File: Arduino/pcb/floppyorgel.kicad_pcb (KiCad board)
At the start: 2 copper layers, 50 x 50 mm, 46 parts, among them J1 VCC_Power_Select, J2 Floppy-Bus, J3 MAX485 Socket, J4 Floppy-Bus, J5 Buck-Converter-5V, J6 Buck-Converter-12V, J7 Floppy-Power, J8 IBM_PC_Floppy_IDC, J9 FTDI, SW1 Bus Address Select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

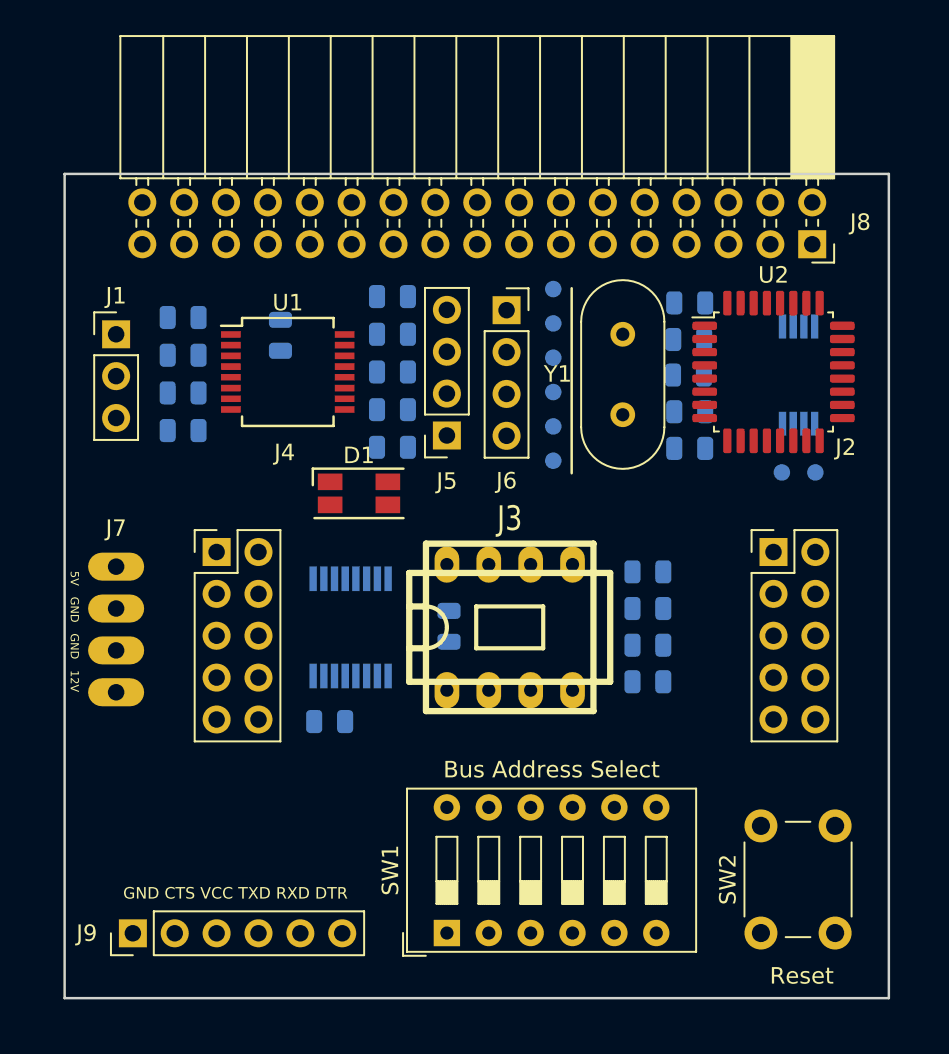
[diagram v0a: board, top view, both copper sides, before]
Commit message: pcb: add logo and zones
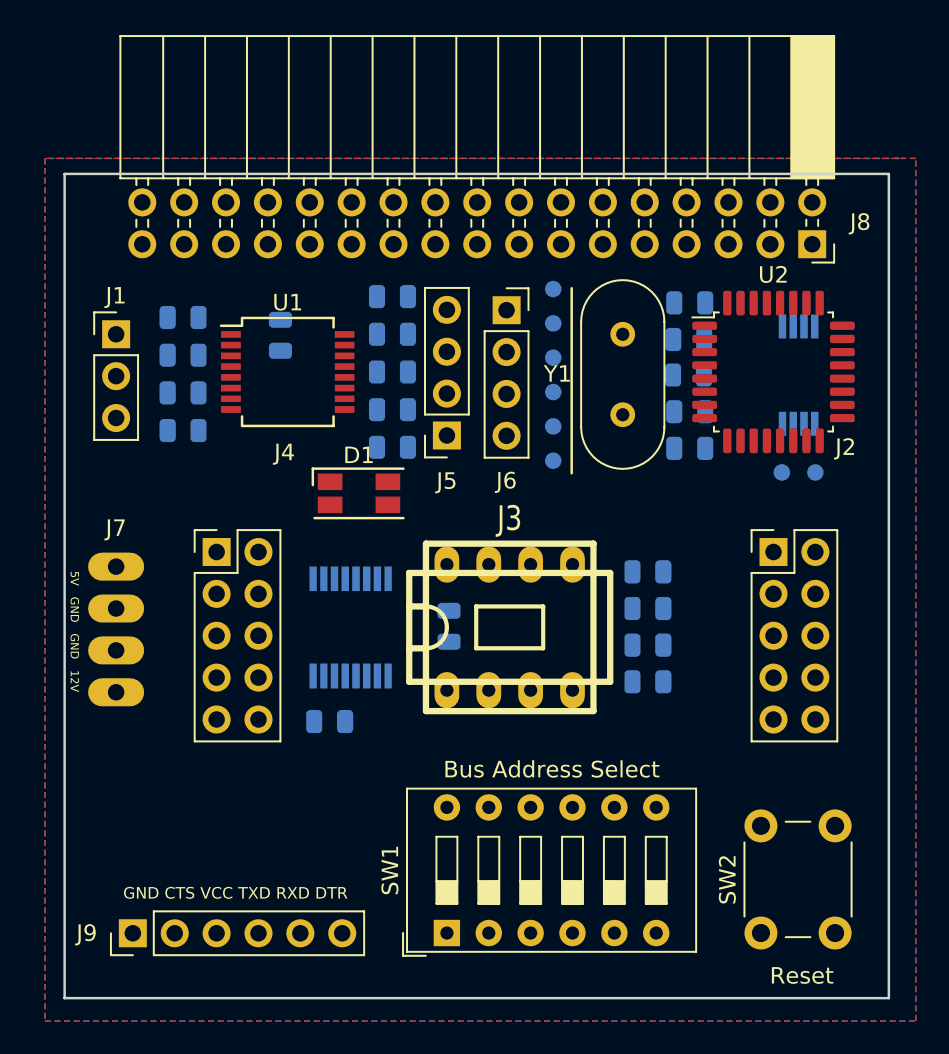
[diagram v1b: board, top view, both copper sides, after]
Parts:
- added G***: LOGO, logo:logo, B.Cu at (109.0, 138.7)
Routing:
- added copper zone on B.Cu, net GND
- added copper zone on F.Cu, net GND

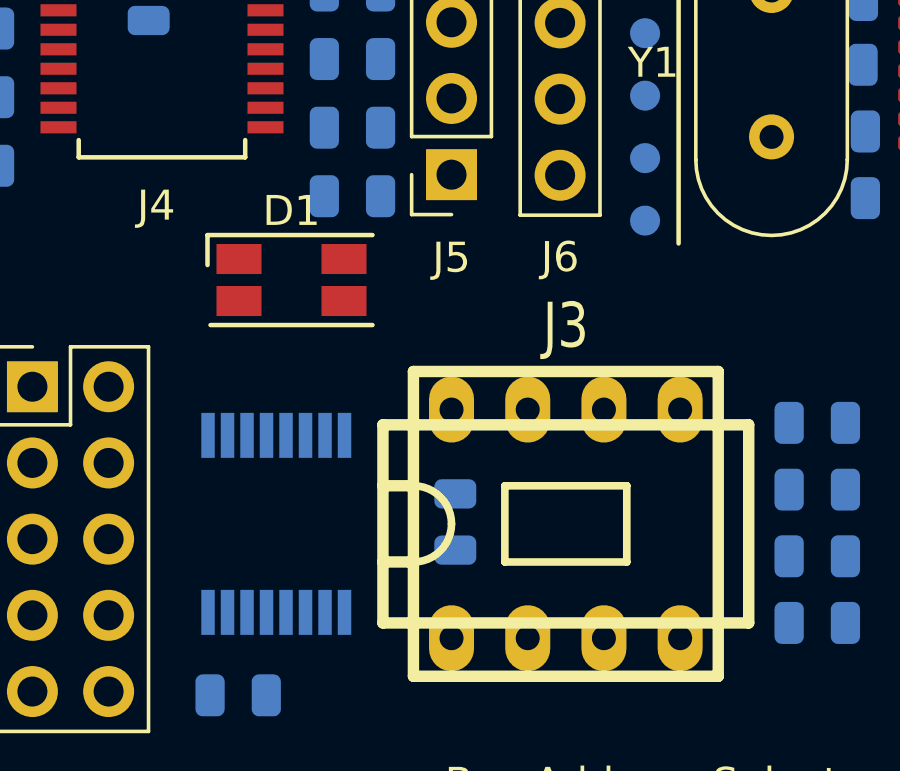
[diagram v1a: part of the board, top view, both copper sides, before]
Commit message: pcb: add missing footprints / add component for logo footprint
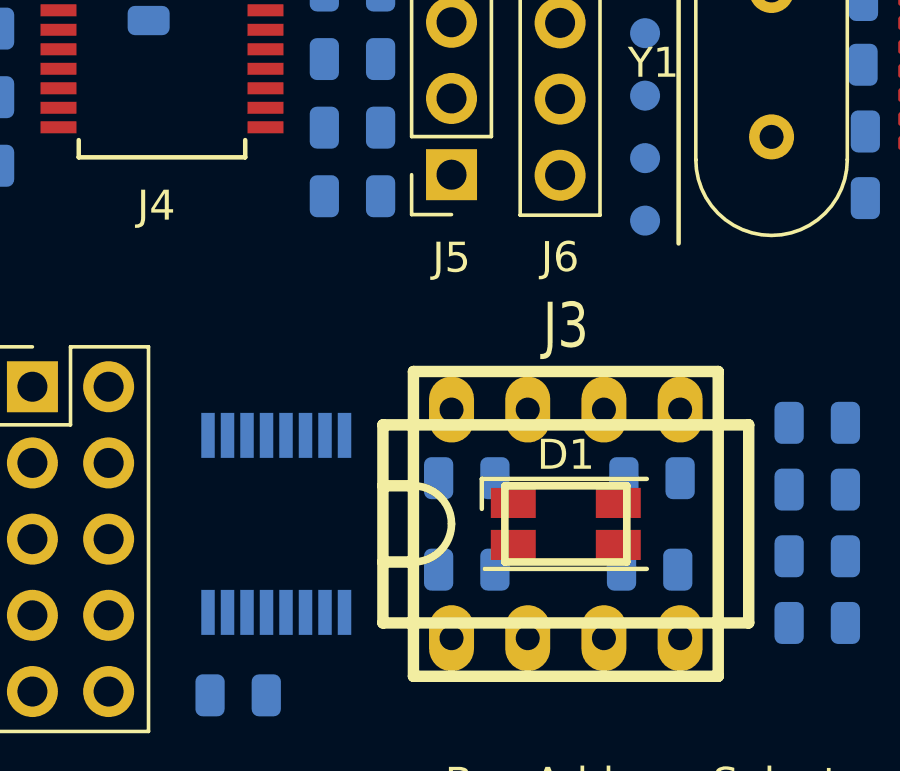
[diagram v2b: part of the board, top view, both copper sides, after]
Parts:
- removed G***: LOGO, logo:logo
- added R14: 250R, Resistor_SMD:R_0805_2012Metric, B.Cu at (123.7, 129.0)
- added R15: 250R, Resistor_SMD:R_0805_2012Metric, B.Cu at (129.8, 129.0)
- added R16: 170R, Resistor_SMD:R_0805_2012Metric, B.Cu at (129.9, 126.0)
- added T1: Logo, logo:logo, B.Cu at (109.5, 138.4)
- moved D1 12.2 mm to (127.0, 127.5)
- moved C1 1.51 mm to (123.7, 126.0), turned to 0 degrees
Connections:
- U4 pad 1: (no net) -> Net-(R15-Pad2)
- U4 pad 15: (no net) -> Net-(R14-Pad2)
- U4 pad 2: Net-(D1-Pad4) -> Net-(R16-Pad2)

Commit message: pcb: fix FTDI and floppy connector orientation
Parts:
- removed T1: Logo, logo:logo
- added L1: logo, logo:logo, B.Cu at (108.2, 138.9)
- J8: footprint Connector_PinSocket_2.54mm:PinSocket_2x17_P2.54mm_Horizontal -> ibm_idc_floppy_connector:ibm_pc_floppy_idc
- moved J8 40.8 mm to (104.6, 101.6), turned to 90 degrees
- moved J9 12.7 mm to (116.8, 146.1), turned to 270 degrees
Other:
- board text added: "DTR RXD TXD VCC CTS GND"
- board text added: "Green Black"
- board text removed: "GND CTS VCC TXD RXD DTR"

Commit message: pcb: add mosfets to RGB led
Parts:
- added Q1: IRLML2060, Package_TO_SOT_SMD:SOT-23, B.Cu at (130.8, 134.9)
- added Q2: IRLML2060, Package_TO_SOT_SMD:SOT-23, B.Cu at (123.2, 134.9)
- added Q3: IRLML2060, Package_TO_SOT_SMD:SOT-23, B.Cu at (127.0, 134.9)
- added R17: 4k7, Resistor_SMD:R_0805_2012Metric, B.Cu at (116.1, 137.4)
- added R18: 4k7, Resistor_SMD:R_0805_2012Metric, B.Cu at (116.1, 139.7)
- added R19: 4k7, Resistor_SMD:R_0805_2012Metric, B.Cu at (116.1, 142.0)
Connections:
- D1 pad 1: GND -> Net-(D1-Pad1)
- D1 pad 2: GND -> Net-(D1-Pad2)
- D1 pad 3: GND -> Net-(D1-Pad3)
- R14 pad 2: Net-(R14-Pad2) -> VCC
- R15 pad 2: Net-(R15-Pad2) -> VCC
- R16 pad 2: Net-(R16-Pad2) -> VCC
- U4 pad 1: Net-(R15-Pad2) -> Net-(Q2-Pad1)
- U4 pad 15: Net-(R14-Pad2) -> Net-(Q1-Pad1)
- U4 pad 2: Net-(R16-Pad2) -> Net-(Q3-Pad1)

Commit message: pcb: add footprint for RGB led
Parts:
- D1: footprint LED_SMD:LED_RGB_1210 -> rgb_led:rgb_led_0805_2012Metric
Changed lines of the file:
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@@
       (effects (font (size 1.5 1.2) (thickness 0.24)))
     )
+    (fp_line (start -6.096 3.302) (end -6.096 -3.302) (layer F.SilkS) (width 0.381))
+    (fp_line (start 6.096 -3.302) (end 6.096 3.302) (layer F.SilkS) (width 0.381))
+    (fp_line (start -5.08 5.08) (end -5.08 -5.08) (layer F.SilkS) (width 0.381))
+    (fp_line (start 5.08 -5.08) (end 5.08 5.08) (layer F.SilkS) (width 0.381))
+    (fp_line (start 2.032 1.27) (end 2.032 -1.27) (layer F.SilkS) (width 0.254))
+    (fp_line (start -2.032 -1.27) (end -2.032 1.27) (layer F.SilkS) (width 0.254))
+    (fp_line (start -5.08 -1.27) (end -6.096 -1.27) (layer F.SilkS) (width 0.381))
+    (fp_line (start -5.08 1.27) (end -6.096 1.27) (layer F.SilkS) (width 0.381))
+    (fp_arc (start -5.08 0) (end -3.81 0) (angle 90) (layer F.SilkS) (width 0.254))
+    (fp_arc (start -5.08 0) (end -5.08 -1.27) (angle 90) (layer F.SilkS) (width 0.254))
+    (fp_line (start -6.096 -3.302) (end 6.096 -3.302) (layer F.SilkS) (width 0.381))
+    (fp_line (start 5.08 -5.08) (end -5.08 -5.08) (layer F.SilkS) (width 0.381))
+    (fp_line (start -6.096 3.302) (end 6.096 3.302) (layer F.SilkS) (width 0.381))
+    (fp_line (start 5.08 5.08) (end -5.08 5.08) (layer F.SilkS) (width 0.381))
+    (fp_line (start -2.032 -1.27) (end 2.032 -1.27) (layer F.SilkS) (width 0.254))
     (fp_line (start 2.032 1.27) (end -2.032 1.27) (layer F.SilkS) (width 0.254))
-    (fp_line (start -2.032 -1.27) (end 2.032 -1.27) (layer F.SilkS) (width 0.254))
-    (fp_line (start 5.08 5.08) (end -5.08 5.08) (layer F.SilkS) (width 0.381))
-    (fp_line (start -6.096 3.302) (end 6.096 3.302) (layer F.SilkS) (width 0.381))
-    (fp_line (start 5.08 -5.08) (end -5.08 -5.08) (layer F.SilkS) (width 0.381))
-    (fp_line (start -6.096 -3.302) (end 6.096 -3.302) (layer F.SilkS) (width 0.381))
-    (fp_arc (start -5.08 0) (end -5.08 -1.27) (angle 90) (layer F.SilkS) (width 0.254))
-    (fp_arc (start -5.08 0) (end -3.81 0) (angle 90) (layer F.SilkS) (width 0.254))
-    (fp_line (start -5.08 1.27) (end -6.096 1.27) (layer F.SilkS) (width 0.381))
-    (fp_line (start -5.08 -1.27) (end -6.096 -1.27) (layer F.SilkS) (width 0.381))
-    (fp_line (start -2.032 -1.27) (end -2.032 1.27) (layer F.SilkS) (width 0.254))
-    (fp_line (start 2.032 1.27) (end 2.032 -1.27) (layer F.SilkS) (width 0.254))
-    (fp_line (start 5.08 -5.08) (end 5.08 5.08) (layer F.SilkS) (width 0.381))
-    (fp_line (start -5.08 5.08) (end -5.08 -5.08) (layer F.SilkS) (width 0.381))
-    (fp_line (start 6.096 -3.302) (end 6.096 3.302) (layer F.SilkS) (width 0.381))
-    (fp_line (start -6.096 3.302) (end -6.096 -3.302) (layer F.SilkS) (width 0.381))
+    (pad 8 thru_hole oval (at -3.81 -3.81) (size 1.5 2.2) (drill 0.8) (layers *.Cu *.Mask F.SilkS)
+      (net 2 VCC))
+    (pad 7 thru_hole oval (at -1.27 -3.81) (size 1.5 2.2) (drill 0.8) (layers *.Cu *.Mask F.SilkS)
+      (net 35 /Bus/BM))
+    (pad 6 thru_hole oval (at 1.27 -3.81) (size 1.5 2.2) (drill 0.8) (layers *.Cu *.Mask F.SilkS)
+      (net 34 /Bus/BP))
+    (pad 5 thru_hole oval (at 3.81 -3.81) (size 1.5 2.2) (drill 0.8) (layers *.Cu *.Mask F.SilkS)
+      (net 3 GND))
+    (pad 4 thru_hole oval (at 3.81 3.81) (size 1.5 2.2) (drill 0.8) (layers *.Cu *.Mask F.SilkS)
+      (net 8 /Bus/RX))
+    (pad 3 thru_hole oval (at 1.27 3.81) (size 1.5 2.2) (drill 0.8) (layers *.Cu *.Mask F.SilkS)
+      (net 3 GND))
+    (pad 2 thru_hole oval (at -1.27 3.81) (size 1.5 2.2) (drill 0.8) (layers *.Cu *.Mask F.SilkS)
+      (net 3 GND))
     (pad 1 thru_hole oval (at -3.81 3.81) (size 1.5 2.2) (drill 0.8) (layers *.Cu *.Mask F.SilkS)
       (net 7 /MCU/RX))
-    (pad 2 thru_hole oval (at -1.27 3.81) (size 1.5 2.2) (drill 0.8) (layers *.Cu *.Mask F.SilkS)
-      (net 3 GND))
-    (pad 3 thru_hole oval (at 1.27 3.81) (size 1.5 2.2) (drill 0.8) (layers *.Cu *.Mask F.SilkS)
-      (net 3 GND))
-    (pad 4 thru_hole oval (at 3.81 3.81) (size 1.5 2.2) (drill 0.8) (layers *.Cu *.Mask F.SilkS)
-      (net 8 /Bus/RX))
-    (pad 5 thru_hole oval (at 3.81 -3.81) (size 1.5 2.2) (drill 0.8) (layers *.Cu *.Mask F.SilkS)
-      (net 3 GND))
-    (pad 6 thru_hole oval (at 1.27 -3.81) (size 1.5 2.2) (drill 0.8) (layers *.Cu *.Mask F.SilkS)
-      (net 34 /Bus/BP))
-    (pad 7 thru_hole oval (at -1.27 -3.81) (size 1.5 2.2) (drill 0.8) (layers *.Cu *.Mask F.SilkS)
-      (net 35 /Bus/BM))
-    (pad 8 thru_hole oval (at -3.81 -3.81) (size 1.5 2.2) (drill 0.8) (layers *.Cu *.Mask F.SilkS)
-      (net 2 VCC))
     (model ${KIPRJMOD}/3d/dil_8-300_socket.wrl
       (at (xyz 0 0 0))
@@
       (net 2 VCC))
     (model ${KISYS3DMOD}/Package_SO.3dshapes/TSSOP-16_4.4x5mm_P0.65mm.wrl
-      (at (xyz 0 0 0))
-      (scale (xyz 1 1 1))
-      (rotate (xyz 0 0 0))
-    )
-  )
-  (module LED_SMD:LED_RGB_1210 (layer F.Cu)
-    (at 127 127.508)
-    (descr "RGB LED 3.2x2.7mm http://www.avagotech.com/docs/AV02-0610EN")
-    (tags "LED 3227")
-    (attr smd)
-    (fp_text reference D1 (at 0 -2.3) (layer F.SilkS)
-      (effects (font (size 1 1) (thickness 0.15)))
-    )
-    (fp_text value LED_RGB (at 0 2.45) (layer F.Fab)
-      (effects (font (size 1 1) (thickness 0.15)))
-    )
-    (fp_line (start -2.95 1.65) (end 2.85 1.65) (layer F.CrtYd) (width 0.05))
-    (fp_line (start -2.95 -1.65) (end -2.95 1.65) (layer F.CrtYd) (width 0.05))
-    (fp_line (start 2.85 -1.65) (end -2.95 -1.65) (layer F.CrtYd) (width 0.05))
-    (fp_line (start 2.85 1.65) (end 2.85 -1.65) (layer F.CrtYd) (width 0.05))
-    (fp_line (start 2.7 1.5) (end -2.7 1.5) (layer F.SilkS) (width 0.15))
-    (fp_line (start 2.7 -1.5) (end -2.8 -1.5) (layer F.SilkS) (width 0.15))
-    (fp_line (start -2.8 -0.5) (end -2.8 -1.5) (layer F.SilkS) (width 0.15))
-    (fp_line (start -0.925 -1.35) (end 1.6 -1.35) (layer F.Fab) (width 0.1))
-    (fp_line (start 1.6 -1.35) (end 1.6 1.35) (layer F.Fab) (width 0.1))
-    (fp_line (start 1.6 1.35) (end -1.6 1.35) (layer F.Fab) (width 0.1))
-    (fp_line (start -1.6 1.35) (end -1.6 -0.675) (layer F.Fab) (width 0.1))
-    (fp_line (start -1.6 -0.675) (end -0.925 -1.35) (layer F.Fab) (width 0.1))
-    (fp_text user %R (at 0 -2.3) (layer F.Fab)
-      (effects (font (size 1 1) (thickness 0.15)))
-    )
-    (pad 1 smd rect (at -1.75 -0.7 180) (size 1.5 1) (layers F.Cu F.Paste F.Mask)
-      (net 36 "Net-(D1-Pad1)"))
-    (pad 2 smd rect (at -1.75 0.7 180) (size 1.5 1) (layers F.Cu F.Paste F.Mask)
-      (net 37 "Net-(D1-Pad2)"))
-    (pad 4 smd rect (at 1.75 -0.7 180) (size 1.5 1) (layers F.Cu F.Paste F.Mask)
-      (net 28 "Net-(D1-Pad4)"))
-    (pad 3 smd rect (at 1.75 0.7 180) (size 1.5 1) (layers F.Cu F.Paste F.Mask)
-      (net 38 "Net-(D1-Pad3)"))
-    (model ${KISYS3DMOD}/LED_SMD.3dshapes/LED_RGB_1210.wrl
       (at (xyz 0 0 0))
       (scale (xyz 1 1 1))
@@
       (at (xyz 0 0 0))
       (scale (xyz 1 1 1))
+      (rotate (xyz 0 0 0))
+    )
+  )
+  (module rgb_led:rgb_led_0805_2012Metric (layer F.Cu)
+    (at 127 127.508)
+    (descr "LED SMD 0805 (2012 Metric), square (rectangular) end terminal, IPC_7351 nominal, (Body size source: https://docs.google.com/spreadsheets/d/1BsfQQcO9C6DZCsRaXUlFlo91Tg2WpOkGARC1WS5S8t0/edit?usp=sharing), generated with kicad-footprint-generator")
+    (tags diode)
+    (attr smd)
+    (fp_text reference D1 (at 0 -1.65) (layer F.SilkS)
+      (effects (font (size 1 1) (thickness 0.15)))
+    )
+    (fp_text value LED_RGB (at 0 1.65) (layer F.Fab)
+      (effects (font (size 1 1) (thickness 0.15)))
+    )
+    (fp_line (start 1 -0.6) (end -0.7 -0.6) (layer F.Fab) (width 0.1))
+    (fp_line (start -0.7 -0.6) (end -1 -0.3) (layer F.Fab) (width 0.1))
+    (fp_line (start -1 -0.3) (end -1 0.6) (layer F.Fab) (width 0.1))
+    (fp_line (start -1 0.6) (end 1 0.6) (layer F.Fab) (width 0.1))
+    (fp_line (start 1 0.6) (end 1 -0.6) (layer F.Fab) (width 0.1))
+    (fp_line (start 1 -0.96) (end -1.685 -0.96) (layer F.SilkS) (width 0.12))
+    (fp_line (start -1.685 -0.96) (end -1.685 0.96) (layer F.SilkS) (width 0.12))
+    (fp_line (start -1.685 0.96) (end 1 0.96) (layer F.SilkS) (width 0.12))
+    (fp_line (start -1.68 0.95) (end -1.68 -0.95) (layer F.CrtYd) (width 0.05))
+    (fp_line (start -1.68 -0.95) (end 1.68 -0.95) (layer F.CrtYd) (width 0.05))
+    (fp_line (start 1.68 -0.95) (end 1.68 0.95) (layer F.CrtYd) (width 0.05))
+    (fp_line (start 1.68 0.95) (end -1.68 0.95) (layer F.CrtYd) (width 0.05))
+    (fp_text user %R (at 0 0) (layer F.Fab)
+      (effects (font (size 0.5 0.5) (thickness 0.08)))
+    )
+    (pad 1 smd rect (at -1.016 -0.4064) (size 1 0.5) (layers F.Cu F.Paste F.Mask)
+      (net 36 "Net-(D1-Pad1)"))
+    (pad 1 smd rect (at -1.016 0.4064) (size 1 0.5) (layers F.Cu F.Paste F.Mask)
+      (net 36 "Net-(D1-Pad1)"))
+    (pad 2 smd rect (at 1.0922 -0.4064) (size 1 0.5) (layers F.Cu F.Paste F.Mask)
+      (net 37 "Net-(D1-Pad2)"))
+    (pad 2 smd rect (at 1.0922 0.4064) (size 1 0.5) (layers F.Cu F.Paste F.Mask)
+      (net 37 "Net-(D1-Pad2)"))
+    (model ${KISYS3DMOD}/LED_SMD.3dshapes/LED_0805_2012Metric.wrl
+      (at (xyz 0 0 0))
+      (scale (xyz 1 1 1))

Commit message: pcb: add switch for VCC power select
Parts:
- J1: footprint Connector_PinHeader_2.54mm:PinHeader_1x03_P2.54mm_Vertical -> w_switch:switch_mmp122-r
- moved J1 2.55 mm to (102.9, 112.3), turned to 270 degrees
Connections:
- Q1 pad 3: Net-(D1-Pad3) -> (no net)
- R16 pad 1: Net-(D1-Pad4) -> (no net)
